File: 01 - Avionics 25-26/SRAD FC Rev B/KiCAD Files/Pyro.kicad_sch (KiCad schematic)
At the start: 0 parts

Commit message: imported pyro from revision A
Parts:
- added C?: 100n, Resistor_SMD:R_0603_1608Metric, symbol Device:C_Small
- added D? (x3): 3V, Package_TO_SOT_SMD:SOT-23, symbol Device:D_Zener
- added F? (x2): 15A, Resistor_SMD:R_1206_3216Metric, symbol Device:Fuse
- added J?: 282834-4, TerminalBlock_TE-Connectivity:TerminalBlock_TE_282834-4_1x04_P2.54mm_Horizontal, symbol Connector:Screw_Terminal_01x04
- added J?: 282834-2, TerminalBlock_TE-Connectivity:TerminalBlock_TE_282834-2_1x02_P2.54mm_Horizontal, symbol Connector:Screw_Terminal_01x02
- added R? (x3): 10K, Resistor_SMD:R_0603_1608Metric, symbol Device:R_Small
- added R? (x3): DNP, Resistor_SMD:R_0603_1608Metric, symbol Device:R_Small
- added R? (x4): 1K, Resistor_SMD:R_0603_1608Metric, symbol Device:R_Small
- added R?: 50m, Resistor_SMD:R_0603_1608Metric, symbol Device:R
- added R?: 1.5k, Resistor_SMD:R_0603_1608Metric, symbol Device:R
- added U?: ZXCT1110W5-7, Package_TO_SOT_SMD:SOT-23-5, symbol Amplifier_Current:ZXCT1110
- added U?: SI9926CDY, Package_SO:SO-8_3.9x4.9mm_P1.27mm, symbol SI9926CDY:SI9926CDY
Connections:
- new net ARMED: D?.3 (K), R?.1, R?.2
- new net CH1-.: F?.1, J?.2 (Pin_2)
- new net CH1-F: F?.2, R?.1, U?.7 (D1), U?.8 (D1)
- new net CH1_DETECT: D?.3 (K), R?.1, R?.2
- new net CH1_FIRE: R?.1, R?.2
- new net CH1_GATE.: R?.1, U?.2 (G1)
- new net CH2-.: F?.1, J?.4 (Pin_4)
- new net CH2-F: F?.2, R?.1, U?.5 (D2), U?.6 (D2)
- new net CH2_DETECT: D?.3 (K), R?.1, R?.2
- new net CH2_FIRE: R?.1, R?.2
- new net CH2_GATE.: R?.1, U?.4 (G2)
- new net CURRENT_SENSE: C?.1, R?.1, U?.3 (OUT)
- new net GND: C?.2, D?.1 (A), D?.1 (A), D?.1 (A), R?.2, R?.2, R?.2, R?.2, R?.2, R?.2, U?.1 (S1), U?.2 (GND), U?.3 (S2)
- new net PYRO_SUPPLY_MONITORED.: J?.1 (Pin_1), J?.3 (Pin_3), R?.2, U?.5 (Vs-)
- new net VBAT: J?.1 (Pin_1)
- new net VBAT_SWITCHED: J?.2 (Pin_2), R?.1, R?.1, U?.4 (Vs+)
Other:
- note added: "Chosen MOSFET: https://www.digikey.com/en/products/detail/vishay-siliconix/SI9926CDY-T1-GE3/1978863 Max Continous FET Current: 8A Max Pulse FET Current: 30A 3.3V_{GS} → R_{DS(ON)} = 17mΩ"
- note added: "EMATCH:"
- note added: "Example Ematch: https://electricmatch.com/pyrotechnics/see/6/5/mjg-firewire-initiator--standard Resistance: 1 +/- 0.2Ω Recommended Current: 1A Minimum Recommended Current: 0.75A Maximum Test Current: 0.04A"
- note added: "FET:"
- note added: "In case of dead short on one pyro channel, an insane amount of current (50A-100A) will be drawn (or attempted). Best case scenario the MCU BOR and everything is okay. Worst case scenario the FET fails closed and the entire board / battery catches fire. The 15A fuses should fail, preventing the above failures from a shorted pyro channel."
- note added: "PYRO CHANNELS AND SENSE"
- note added: "https://www.rocketryforum.com/threads/minimum-all-fire-energy-of-mjg-technologies-firewire-initiator.138423/"
- company: (none) -> Missouri S&T Rocket Design Team
- title: (none) -> Pyro Channels

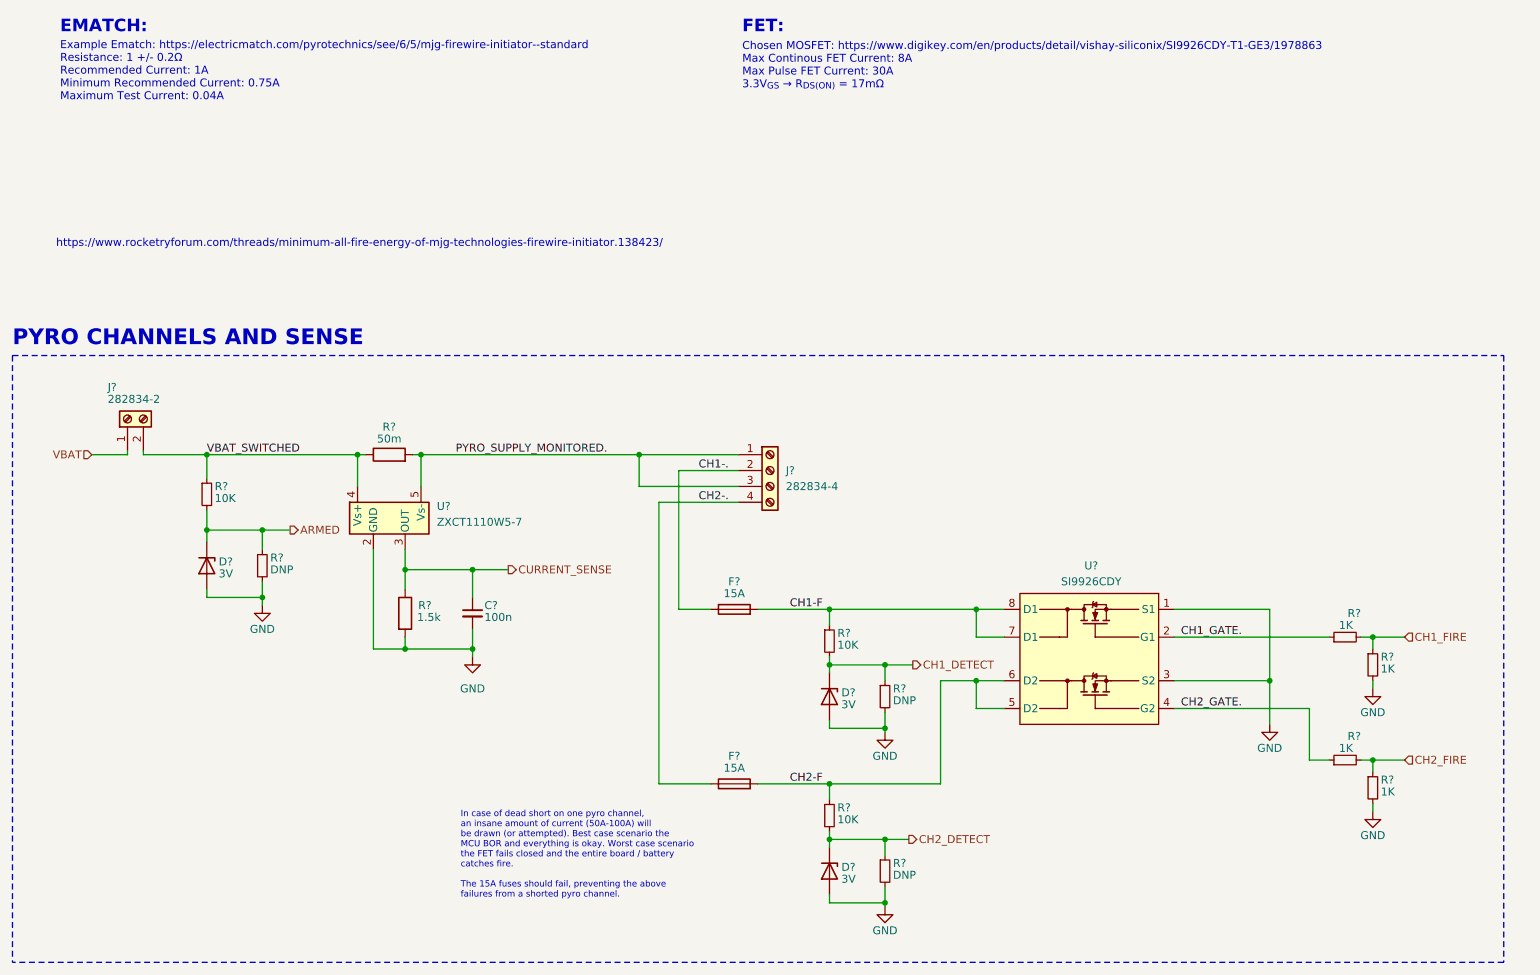
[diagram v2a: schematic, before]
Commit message: general fixes for sheet sheet, ERC error fixes
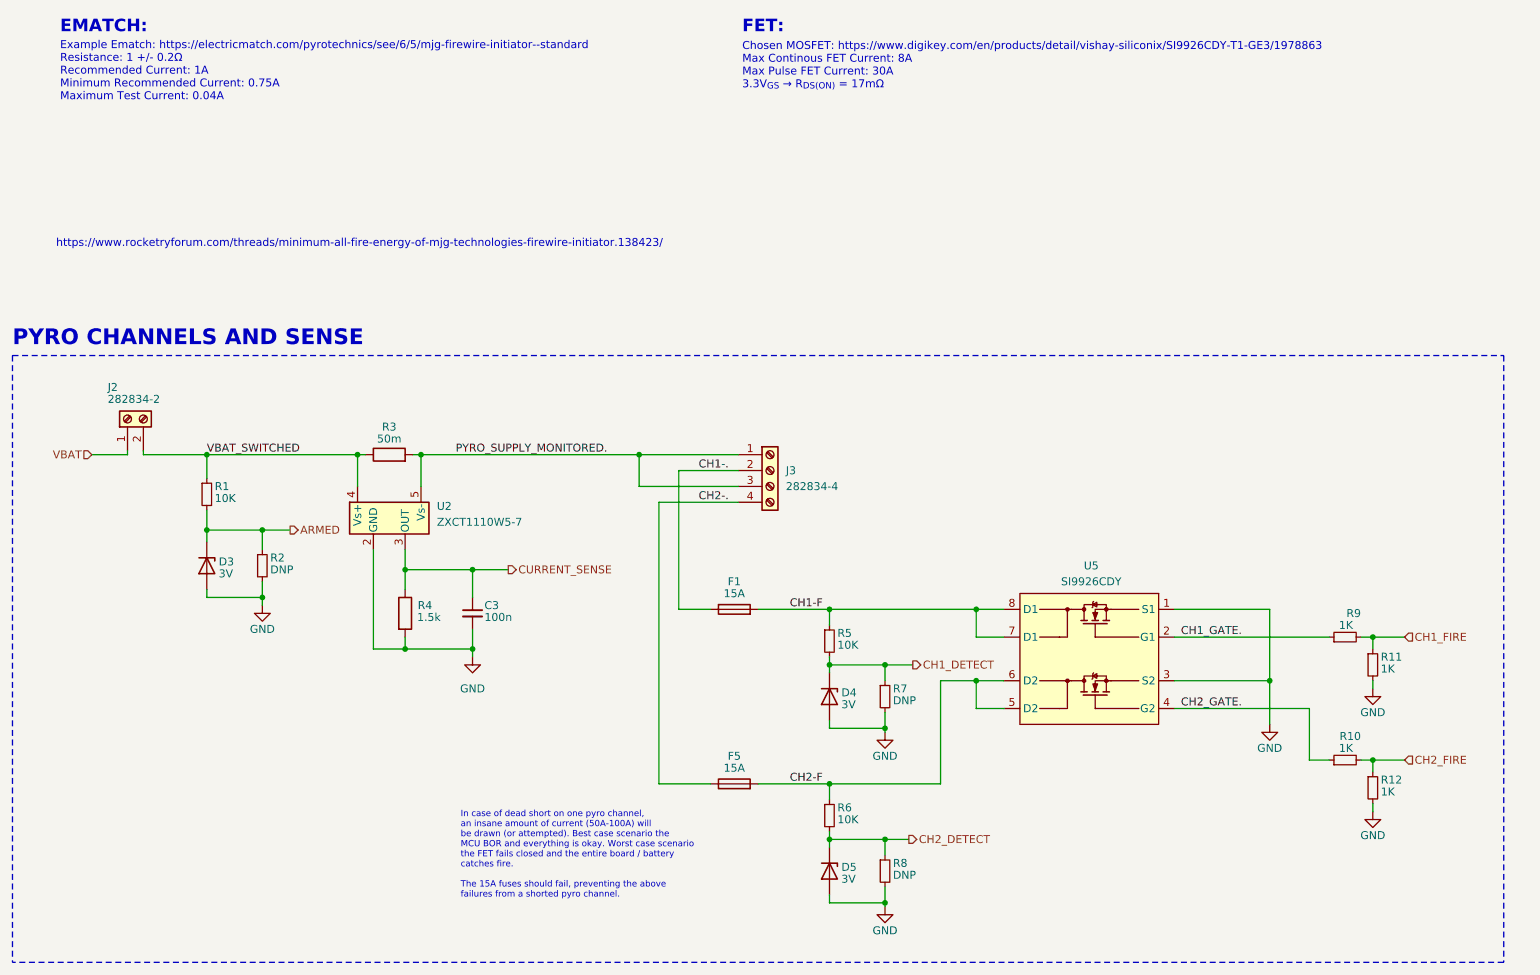
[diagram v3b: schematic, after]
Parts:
- gave numbers to parts that had none: 22
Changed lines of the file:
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@@
 		(on_board yes)
 		(dnp no)
-		(property "Reference" "R?"
+		(property "Reference" "R1"
 			(at 51.435 93.345 0)
 			(effects
@@
 			(project "SRAD FC Rev B"
 				(path "/1dd9e63a-24f2-43c6-ae21-66b89e6998f2/9d37d36a-f460-49db-aaa9-575118e1aeb1"
-					(reference "R?")
+					(reference "R1")
 					(unit 1)
 				)
@@
 		(on_board yes)
 		(dnp no)
-		(property "Reference" "R?"
+		(property "Reference" "R2"
 			(at 60.325 104.775 0)
 			(effects
@@
 			(project "SRAD FC Rev B"
 				(path "/1dd9e63a-24f2-43c6-ae21-66b89e6998f2/9d37d36a-f460-49db-aaa9-575118e1aeb1"
-					(reference "R?")
+					(reference "R2")
 					(unit 1)
 				)
@@
 		(on_board yes)
 		(dnp no)
-		(property "Reference" "R?"
+		(property "Reference" "R5"
 			(at 151.13 116.84 0)
 			(effects
@@
 			(project "SRAD FC Rev B"
 				(path "/1dd9e63a-24f2-43c6-ae21-66b89e6998f2/9d37d36a-f460-49db-aaa9-575118e1aeb1"
-					(reference "R?")
+					(reference "R5")
 					(unit 1)
 				)
@@
 		(on_board yes)
 		(dnp no)
-		(property "Reference" "R?"
+		(property "Reference" "R11"
 			(at 238.125 120.65 0)
 			(effects
@@
 			(project "SRAD FC Rev B"
 				(path "/1dd9e63a-24f2-43c6-ae21-66b89e6998f2/9d37d36a-f460-49db-aaa9-575118e1aeb1"
-					(reference "R?")
+					(reference "R11")
 					(unit 1)
 				)
@@
 		(on_board yes)
 		(dnp no)
-		(property "Reference" "D?"
+		(property "Reference" "D3"
 			(at 52.07 105.41 90)
 			(effects
@@
 			(project "SRAD FC Rev B"
 				(path "/1dd9e63a-24f2-43c6-ae21-66b89e6998f2/9d37d36a-f460-49db-aaa9-575118e1aeb1"
-					(reference "D?")
+					(reference "D3")
 					(unit 1)
 				)
@@
 		(on_board yes)
 		(dnp no)
-		(property "Reference" "R?"
+		(property "Reference" "R12"
 			(at 238.125 140.335 0)
 			(effects
@@
 			(project "SRAD FC Rev B"
 				(path "/1dd9e63a-24f2-43c6-ae21-66b89e6998f2/9d37d36a-f460-49db-aaa9-575118e1aeb1"
-					(reference "R?")
+					(reference "R12")
 					(unit 1)
 				)
@@
 		(on_board yes)
 		(dnp no)
-		(property "Reference" "J?"
+		(property "Reference" "J3"
 			(at 142.875 90.805 0)
 			(effects
@@
 			(project "SRAD FC Rev B"
 				(path "/1dd9e63a-24f2-43c6-ae21-66b89e6998f2/9d37d36a-f460-49db-aaa9-575118e1aeb1"
-					(reference "J?")
+					(reference "J3")
 					(unit 1)
 				)
@@
 		(on_board yes)
 		(dnp no)
-		(property "Reference" "R?"
+		(property "Reference" "R9"
 			(at 234.95 113.665 90)
 			(effects
@@
 			(project "SRAD FC Rev B"
 				(path "/1dd9e63a-24f2-43c6-ae21-66b89e6998f2/9d37d36a-f460-49db-aaa9-575118e1aeb1"
-					(reference "R?")
+					(reference "R9")
 					(unit 1)
 				)
@@
 		(on_board yes)
 		(dnp no)
-		(property "Reference" "R?"
+		(property "Reference" "R7"
 			(at 160.02 125.73 0)
 			(effects
@@
 			(project "SRAD FC Rev B"
 				(path "/1dd9e63a-24f2-43c6-ae21-66b89e6998f2/9d37d36a-f460-49db-aaa9-575118e1aeb1"
-					(reference "R?")
+					(reference "R7")
 					(unit 1)
 				)
@@
 		(on_board yes)
 		(dnp no)
-		(property "Reference" "R?"
+		(property "Reference" "R10"
 			(at 234.95 133.35 90)
 			(effects
@@
 			(project "SRAD FC Rev B"
 				(path "/1dd9e63a-24f2-43c6-ae21-66b89e6998f2/9d37d36a-f460-49db-aaa9-575118e1aeb1"
-					(reference "R?")
+					(reference "R10")
 					(unit 1)
 				)
@@
 		(on_board yes)
 		(dnp no)
-		(property "Reference" "U?"
+		(property "Reference" "U2"
 			(at 86.995 96.52 0)
 			(effects
@@
 			(project "SRAD FC Rev B"
 				(path "/1dd9e63a-24f2-43c6-ae21-66b89e6998f2/9d37d36a-f460-49db-aaa9-575118e1aeb1"
-					(reference "U?")
+					(reference "U2")
 					(unit 1)
 				)
@@
 		(on_board yes)
 		(dnp no)
-		(property "Reference" "D?"
+		(property "Reference" "D5"
 			(at 151.765 154.305 90)
 			(effects
@@
 			(project "SRAD FC Rev B"
 				(path "/1dd9e63a-24f2-43c6-ae21-66b89e6998f2/9d37d36a-f460-49db-aaa9-575118e1aeb1"
-					(reference "D?")
+					(reference "D5")
 					(unit 1)
 				)
@@
 		(on_board yes)
 		(dnp no)
-		(property "Reference" "R?"
+		(property "Reference" "R8"
 			(at 160.02 153.67 0)
 			(effects
@@
 			(project "SRAD FC Rev B"
 				(path "/1dd9e63a-24f2-43c6-ae21-66b89e6998f2/9d37d36a-f460-49db-aaa9-575118e1aeb1"
-					(reference "R?")
+					(reference "R8")
 					(unit 1)
 				)
@@
 		(on_board yes)
 		(dnp no)
-		(property "Reference" "D?"
+		(property "Reference" "D4"
 			(at 151.765 126.365 90)
 			(effects
@@
 			(project "SRAD FC Rev B"
 				(path "/1dd9e63a-24f2-43c6-ae21-66b89e6998f2/9d37d36a-f460-49db-aaa9-575118e1aeb1"
-					(reference "D?")
+					(reference "D4")
 					(unit 1)
 				)
@@
 		(on_board yes)
 		(dnp no)
-		(property "Reference" "J?"
+		(property "Reference" "J2"
 			(at 34.29 77.47 90)
 			(effects
@@
 			(project "SRAD FC Rev B"
 				(path "/1dd9e63a-24f2-43c6-ae21-66b89e6998f2/9d37d36a-f460-49db-aaa9-575118e1aeb1"
-					(reference "J?")
+					(reference "J2")
 					(unit 1)
 				)
@@
 		(on_board yes)
 		(dnp no)
-		(property "Reference" "F?"
+		(property "Reference" "F1"
 			(at 134.62 108.585 90)
 			(effects
@@
 			(project "SRAD FC Rev B"
 				(path "/1dd9e63a-24f2-43c6-ae21-66b89e6998f2/9d37d36a-f460-49db-aaa9-575118e1aeb1"
-					(reference "F?")
+					(reference "F1")
 					(unit 1)
 				)
@@
 		(on_board yes)
 		(dnp no)
-		(property "Reference" "C?"
+		(property "Reference" "C3"
 			(at 94.615 112.395 0)
 			(effects
@@
 			(project "SRAD FC Rev B"
 				(path "/1dd9e63a-24f2-43c6-ae21-66b89e6998f2/9d37d36a-f460-49db-aaa9-575118e1aeb1"
-					(reference "C?")
+					(reference "C3")
 					(unit 1)
 				)
@@
 		(on_board yes)
 		(dnp no)
-		(property "Reference" "R?"
+		(property "Reference" "R3"
 			(at 79.375 83.82 90)
 			(effects
@@
 			(project "SRAD FC Rev B"
 				(path "/1dd9e63a-24f2-43c6-ae21-66b89e6998f2/9d37d36a-f460-49db-aaa9-575118e1aeb1"
-					(reference "R?")
+					(reference "R3")
 					(unit 1)
 				)
@@
 		(on_board yes)
 		(dnp no)
-		(property "Reference" "F?"
+		(property "Reference" "F5"
 			(at 134.62 136.525 90)
 			(effects
@@
 			(project "SRAD FC Rev B"
 				(path "/1dd9e63a-24f2-43c6-ae21-66b89e6998f2/9d37d36a-f460-49db-aaa9-575118e1aeb1"
-					(reference "F?")
+					(reference "F5")
 					(unit 1)
 				)
@@
 		(on_board yes)
 		(dnp no)
-		(property "Reference" "R?"
+		(property "Reference" "R6"
 			(at 151.13 144.78 0)
 			(effects
@@
 			(project "SRAD FC Rev B"
 				(path "/1dd9e63a-24f2-43c6-ae21-66b89e6998f2/9d37d36a-f460-49db-aaa9-575118e1aeb1"
-					(reference "R?")
+					(reference "R6")
 					(unit 1)
 				)
@@
 		(on_board yes)
 		(dnp no)
-		(property "Reference" "U?"
+		(property "Reference" "U5"
 			(at 191.77 106.045 0)
 			(effects
@@
 			(project "SRAD FC Rev B"
 				(path "/1dd9e63a-24f2-43c6-ae21-66b89e6998f2/9d37d36a-f460-49db-aaa9-575118e1aeb1"
-					(reference "U?")
+					(reference "U5")
 					(unit 1)
 				)
@@
 		(on_board yes)
 		(dnp no)
-		(property "Reference" "R?"
+		(property "Reference" "R4"
 			(at 85.09 112.395 0)
 			(effects
@@
 			(project "SRAD FC Rev B"
 				(path "/1dd9e63a-24f2-43c6-ae21-66b89e6998f2/9d37d36a-f460-49db-aaa9-575118e1aeb1"
-					(reference "R?")
-					(unit 1)
-				)
+					(reference "R4")
+					(unit 1)
+				)

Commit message: some fixes from seth's feedback
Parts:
- removed C3: 100n, Resistor_SMD:R_0603_1608Metric, symbol Device:C_Small
- removed R3: 50m, Resistor_SMD:R_0603_1608Metric, symbol Device:R
- removed R4: 1.5k, Resistor_SMD:R_0603_1608Metric, symbol Device:R
- removed U2: ZXCT1110W5-7, Package_TO_SOT_SMD:SOT-23-5, symbol Amplifier_Current:ZXCT1110
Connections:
- net VBAT_SWITCHED is gone; now on net PYRO_SUPPLY.: J2.2 (Pin_2), R1.1
- net PYRO_SUPPLY_MONITORED. renamed PYRO_SUPPLY.
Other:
- moved on the sheet: D3, D4, D5, F1, F5, J2, J3, R1, R10, R11, R12, R2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
